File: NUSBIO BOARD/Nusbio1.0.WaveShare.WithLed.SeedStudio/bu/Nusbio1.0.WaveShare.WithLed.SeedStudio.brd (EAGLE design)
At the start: 40.1 x 84 mm, 13 parts

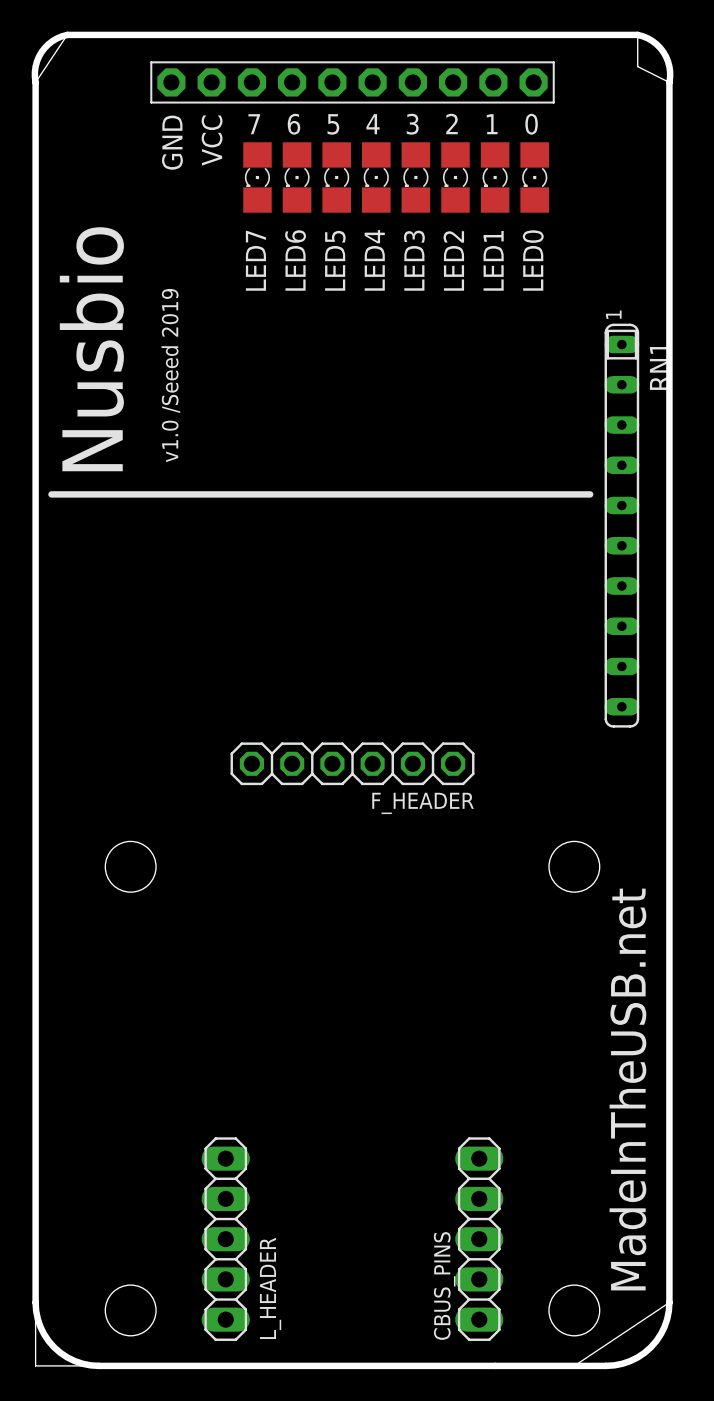
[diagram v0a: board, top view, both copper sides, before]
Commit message: New board Nusbio WaveShare SeedStudio edition larger with 8 blue 1206 led
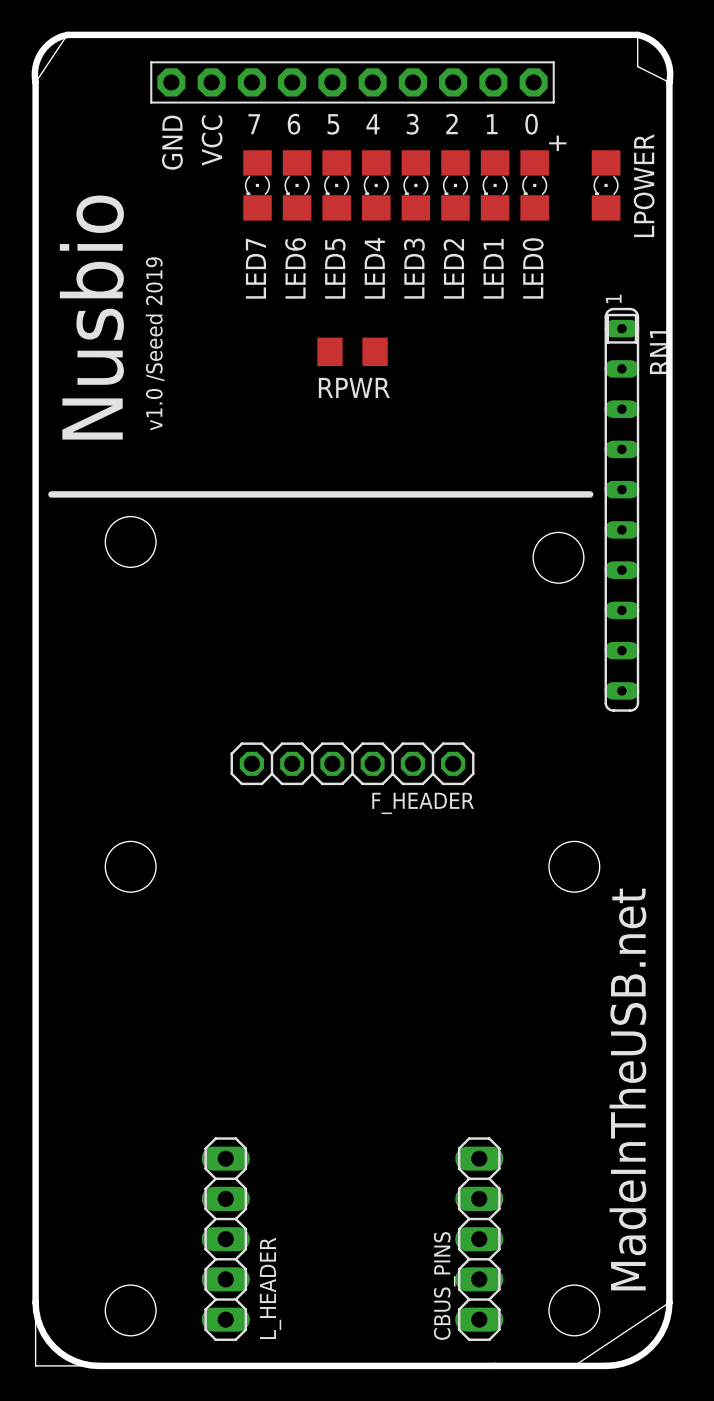
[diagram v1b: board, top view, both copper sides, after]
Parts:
- added LPOWER: (no value), adafruit:1206
- added RPWR: (no value), adafruit:R1206
- moved RN1 1.00 mm to (38.0, 54.0)
- moved LED0 0.50 mm to (32.5, 74.5)
- moved LED1 0.50 mm to (30.0, 74.5)
- moved LED2 0.50 mm to (27.5, 74.5)
- moved LED3 0.50 mm to (25.0, 74.5)
- moved LED4 0.50 mm to (22.5, 74.5)
- moved LED5 0.50 mm to (20.0, 74.5)
- moved LED6 0.50 mm to (17.5, 74.5)
- moved LED7 0.50 mm to (15.0, 74.5)
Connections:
- new net N$9: LPOWER.C, RPWR.1
- net GND: now also RPWR.2
- net NUSBIO_VCC: now also LPOWER.A
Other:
- board text added: "+"

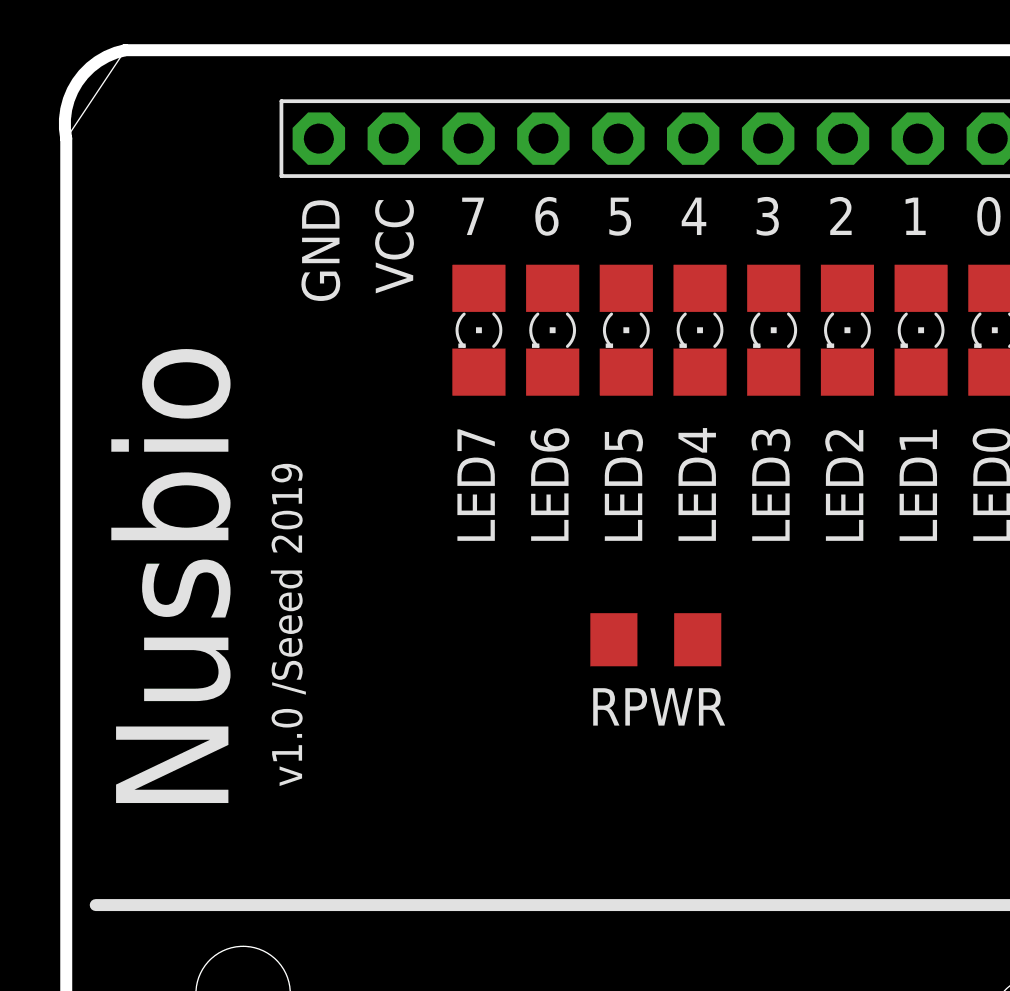
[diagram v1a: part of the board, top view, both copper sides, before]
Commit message: board 4017-7Segment v2 on hold, until I received chip 4017B
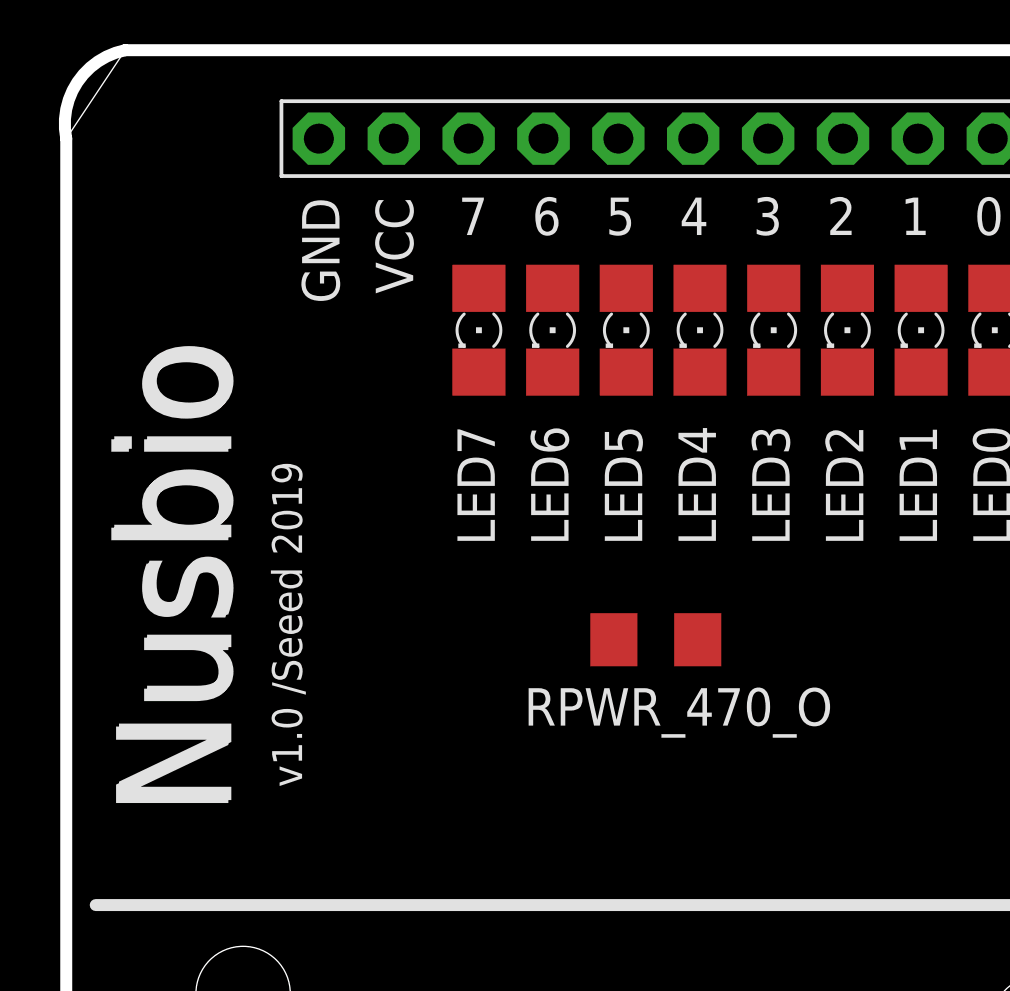
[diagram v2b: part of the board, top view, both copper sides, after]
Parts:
- renumbered RPWR to RPWR_470_O
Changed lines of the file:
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@@
 <hole x="7" y="52" drill="3.2"/>
 <text x="34.5" y="76.5" size="1.27" layer="25" rot="R90">+</text>
+<text x="6.6" y="58.1" size="3.81" layer="25" rot="R90">Nusbio</text>
 </plain>
 <attributes>
@@
 <attribute name="VALUE" x="34.46" y="75.77" size="1.27" layer="27" rot="R270"/>
 </element>
-<element name="RPWR" library="adafruit" package="R1206" value="" x="21" y="64" smashed="yes" rot="R180">
-<attribute name="NAME" x="23.397" y="62.357" size="1.27" layer="25" rot="R180"/>
+<element name="RPWR_470_O" library="adafruit" package="R1206" value="" x="21" y="64" smashed="yes" rot="R180">
+<attribute name="NAME" x="27" y="62.357" size="1.27" layer="25" rot="R180"/>
 <attribute name="VALUE" x="22.397" y="66.413" size="1.27" layer="27" rot="R180"/>
 </element>
@@
 <contactref element="F_HEADER" pad="2"/>
 <contactref element="RN1" pad="1"/>
-<contactref element="RPWR" pad="2"/>
+<contactref element="RPWR_470_O" pad="2"/>
 <wire x1="19.578" y1="64" x2="38" y2="65.46" width="0" layer="19" extent="1-1"/>
 <wire x1="9.57" y1="81" x2="19.578" y2="64" width="0" layer="19" extent="1-1"/>
@@
 <signal name="N$9">
 <contactref element="LPOWER" pad="C"/>
-<contactref element="RPWR" pad="1"/>
+<contactref element="RPWR_470_O" pad="1"/>
 <wire x1="22.422" y1="64" x2="37" y2="73.078" width="0" layer="19" extent="1-1"/>
 </signal>
